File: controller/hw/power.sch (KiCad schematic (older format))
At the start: 12 parts, among them P401 WAGO255, Q401 IRFU9024, U401 Mini-360, U402 Mini-360

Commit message: Restructure files and small updates
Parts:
- added C?: C, symbol C
- added R?: 12k, symbol R
- added R?: 10k, symbol R
- added R?: R, symbol R
- added U?: TL431ACD, symbol TL431ACD
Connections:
- wire segments 40 -> 57
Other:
- note added: "Overvoltage crowbar protection"
- note added: "Triak, MT1 nahoře\nnapř. Z0103MA 5AL2"
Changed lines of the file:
@@
 	1    0    0    -1
 $EndComp
-Text HLabel 7000 1200 2    60   UnSpc ~ 0
+Text HLabel 10250 1200 2    60   UnSpc ~ 0
 +5V
 Text HLabel 7000 2600 2    60   UnSpc ~ 0
 +12V
-Text HLabel 7000 3450 2    60   UnSpc ~ 0
+Text HLabel 10250 3450 2    60   UnSpc ~ 0
 GND
 Text Notes 4950 1650 0    60   ~ 0
@@
 Connection ~ 4200 2050
 Wire Wire Line
-	4450 1800 4450 3450
+	4450 3450 4450 1800
 Wire Wire Line
 	4450 1800 4600 1800
@@
 	6300 3450 6300 2950
 Wire Wire Line
-	7000 1200 5650 1200
-Wire Wire Line
-	3050 3450 7000 3450
+	10250 1200 5650 1200
+Wire Wire Line
+	3050 3450 10250 3450
 Connection ~ 5650 3450
 Wire Wire Line
@@
 	3600 2900 3600 3450
 Connection ~ 3600 3450
+$Comp
+L TL431ACD U?
+U 1 1 5925D1B0
+P 8700 2250
+F 0 "U?" H 9088 2303 60  0000 L CNN
+F 1 "TL431ACD" H 9088 2197 60  0000 L CNN
+F 2 "" H 9550 2100 60  0001 C CNN
+F 3 "" H 9550 2100 60  0001 C CNN
+	1    8700 2250
+	1    0    0    -1
+$EndComp
+$Comp
+L R R?
+U 1 1 5925D21E
+P 8000 1950
+F 0 "R?" H 8070 1996 50  0000 L CNN
+F 1 "12k" H 8070 1905 50  0000 L CNN
+F 2 "" V 7930 1950 30  0000 C CNN
+F 3 "" H 8000 1950 30  0000 C CNN
+	1    8000 1950
+	1    0    0    -1
+$EndComp
+$Comp
+L R R?
+U 1 1 5925D25E
+P 8000 2350
+F 0 "R?" H 8070 2396 50  0000 L CNN
+F 1 "10k" H 8070 2305 50  0000 L CNN
+F 2 "" V 7930 2350 30  0000 C CNN
+F 3 "" H 8000 2350 30  0000 C CNN
+	1    8000 2350
+	1    0    0    -1
+$EndComp
+$Comp
+L R R?
+U 1 1 5925D32B
+P 8900 1600
+F 0 "R?" H 8970 1646 50  0000 L CNN
+F 1 "R" H 8970 1555 50  0000 L CNN
+F 2 "" V 8830 1600 30  0000 C CNN
+F 3 "" H 8900 1600 30  0000 C CNN
+	1    8900 1600
+	1    0    0    -1
+$EndComp
+Wire Wire Line
+	8300 2150 8000 2150
+Wire Wire Line
+	8000 2100 8000 2200
+Connection ~ 8000 2150
+Wire Wire Line
+	8000 2500 8000 2800
+Wire Wire Line
+	8000 2800 9350 2800
+Wire Wire Line
+	9000 2800 9000 2650
+Wire Wire Line
+	8550 2800 8550 3450
+Connection ~ 8550 3450
+Connection ~ 8550 2800
+Wire Wire Line
+	8700 2650 8700 2800
+Connection ~ 8700 2800
+Wire Wire Line
+	8800 2650 8800 2800
+Connection ~ 8800 2800
+Wire Wire Line
+	8900 2650 8900 2800
+Connection ~ 8900 2800
+Wire Wire Line
+	8000 1800 8000 1350
+Wire Wire Line
+	8000 1350 9850 1350
+Wire Wire Line
+	8900 1450 8900 1350
+Connection ~ 8900 1350
+Wire Wire Line
+	8900 1750 8900 1850
+Wire Wire Line
+	8900 1800 9550 1800
+Connection ~ 8900 1800
+Wire Wire Line
+	8550 1350 8550 1200
+Connection ~ 8550 1200
+Connection ~ 8550 1350
+Text Notes 7900 1100 0    60   ~ 0
+Overvoltage crowbar protection
+$Comp
+L C C?
+U 1 1 5925DDF5
+P 9350 2600
+F 0 "C?" H 9465 2646 50  0000 L CNN
+F 1 "C" H 9465 2555 50  0000 L CNN
+F 2 "" H 9388 2450 30  0000 C CNN
+F 3 "" H 9350 2600 60  0000 C CNN
+	1    9350 2600
+	1    0    0    -1
+$EndComp
+Wire Wire Line
+	9350 2450 9350 1800
+Connection ~ 9350 1800
+Wire Wire Line
+	9350 2800 9350 2750
+Connection ~ 9000 2800
+Text Notes 9900 2350 0    60   ~ 0
+Triak, MT1 nahoře\nnapř. Z0103MA 5AL2
 $EndSCHEMATC

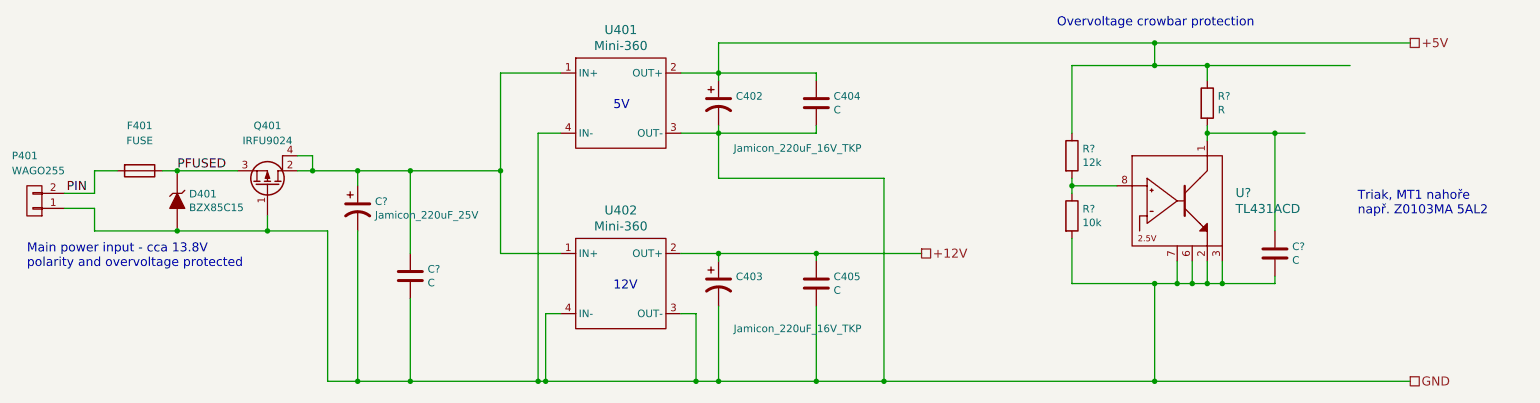
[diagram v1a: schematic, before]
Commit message: Fix voltage for SPI flash, short under one capacitor
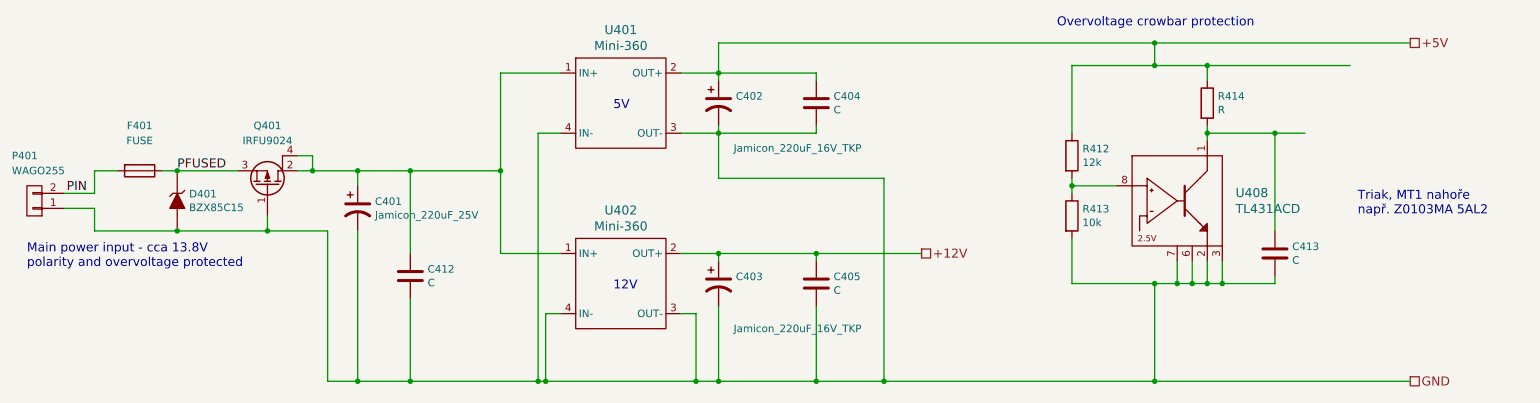
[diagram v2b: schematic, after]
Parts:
- gave numbers to parts that had none: 7
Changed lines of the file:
@@
 $EndComp
 $Comp
-L Jamicon_220uF_25V C?
+L Jamicon_220uF_25V C401
 U 1 1 5922BD9A
 P 3250 2300
-F 0 "C?" H 3365 2346 50  0000 L CNN
+F 0 "C401" H 3365 2346 50  0000 L CNN
 F 1 "Jamicon_220uF_25V" H 3365 2255 50  0000 L CNN
 F 2 "" H 3250 2300 60  0000 C CNN
@@
 $EndComp
 $Comp
-L C C?
+L C C412
 U 1 1 5922BEB6
 P 3600 2750
-F 0 "C?" H 3715 2796 50  0000 L CNN
+F 0 "C412" H 3715 2796 50  0000 L CNN
 F 1 "C" H 3715 2705 50  0000 L CNN
 F 2 "" H 3638 2600 30  0000 C CNN
@@
 Connection ~ 3600 3450
 $Comp
-L TL431ACD U?
+L TL431ACD U408
 U 1 1 5925D1B0
 P 8700 2250
-F 0 "U?" H 9088 2303 60  0000 L CNN
+F 0 "U408" H 9088 2303 60  0000 L CNN
 F 1 "TL431ACD" H 9088 2197 60  0000 L CNN
 F 2 "" H 9550 2100 60  0001 C CNN
@@
 $EndComp
 $Comp
-L R R?
+L R R412
 U 1 1 5925D21E
 P 8000 1950
-F 0 "R?" H 8070 1996 50  0000 L CNN
+F 0 "R412" H 8070 1996 50  0000 L CNN
 F 1 "12k" H 8070 1905 50  0000 L CNN
 F 2 "" V 7930 1950 30  0000 C CNN
@@
 $EndComp
 $Comp
-L R R?
+L R R413
 U 1 1 5925D25E
 P 8000 2350
-F 0 "R?" H 8070 2396 50  0000 L CNN
+F 0 "R413" H 8070 2396 50  0000 L CNN
 F 1 "10k" H 8070 2305 50  0000 L CNN
 F 2 "" V 7930 2350 30  0000 C CNN
@@
 $EndComp
 $Comp
-L R R?
+L R R414
 U 1 1 5925D32B
 P 8900 1600
-F 0 "R?" H 8970 1646 50  0000 L CNN
+F 0 "R414" H 8970 1646 50  0000 L CNN
 F 1 "R" H 8970 1555 50  0000 L CNN
 F 2 "" V 8830 1600 30  0000 C CNN
@@
 Overvoltage crowbar protection
 $Comp
-L C C?
+L C C413
 U 1 1 5925DDF5
 P 9350 2600
-F 0 "C?" H 9465 2646 50  0000 L CNN
+F 0 "C413" H 9465 2646 50  0000 L CNN
 F 1 "C" H 9465 2555 50  0000 L CNN
 F 2 "" H 9388 2450 30  0000 C CNN

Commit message: Save latest changes to sch
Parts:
- C401: footprint (none) -> th-normal:C_Radial_D8_L11.5_P3.5
- C412, C413: footprint (none) -> smd-handsolder:C_1206_HandSoldering
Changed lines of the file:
@@
 F 0 "C401" H 3365 2346 50  0000 L CNN
 F 1 "Jamicon_220uF_25V" H 3365 2255 50  0000 L CNN
-F 2 "" H 3250 2300 60  0000 C CNN
+F 2 "th-normal:C_Radial_D8_L11.5_P3.5" H 3250 2300 60  0001 C CNN
 F 3 "" H 3250 2300 60  0000 C CNN
 	1    3250 2300
@@
 F 0 "C412" H 3715 2796 50  0000 L CNN
 F 1 "C" H 3715 2705 50  0000 L CNN
-F 2 "" H 3638 2600 30  0000 C CNN
+F 2 "smd-handsolder:C_1206_HandSoldering" H 3638 2600 30  0001 C CNN
 F 3 "" H 3600 2750 60  0000 C CNN
 	1    3600 2750
@@
 F 0 "R412" H 8070 1996 50  0000 L CNN
 F 1 "12k" H 8070 1905 50  0000 L CNN
-F 2 "" V 7930 1950 30  0000 C CNN
+F 2 "" V 7930 1950 30  0001 C CNN
 F 3 "" H 8000 1950 30  0000 C CNN
 	1    8000 1950
@@
 F 0 "R413" H 8070 2396 50  0000 L CNN
 F 1 "10k" H 8070 2305 50  0000 L CNN
-F 2 "" V 7930 2350 30  0000 C CNN
+F 2 "" V 7930 2350 30  0001 C CNN
 F 3 "" H 8000 2350 30  0000 C CNN
 	1    8000 2350
@@
 F 0 "R414" H 8970 1646 50  0000 L CNN
 F 1 "R" H 8970 1555 50  0000 L CNN
-F 2 "" V 8830 1600 30  0000 C CNN
+F 2 "" V 8830 1600 30  0001 C CNN
 F 3 "" H 8900 1600 30  0000 C CNN
 	1    8900 1600
@@
 F 0 "C413" H 9465 2646 50  0000 L CNN
 F 1 "C" H 9465 2555 50  0000 L CNN
-F 2 "" H 9388 2450 30  0000 C CNN
+F 2 "smd-handsolder:C_1206_HandSoldering" H 9388 2450 30  0001 C CNN
 F 3 "" H 9350 2600 60  0000 C CNN
 	1    9350 2600

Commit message: Compilability using embc lm4f, fixes to TX_EN switching
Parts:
- C401: symbol Jamicon_220uF_25V -> capacitors:Jamicon_220uF_25V
- C402, C403: symbol Jamicon_220uF_16V_TKP -> capacitors:Jamicon_220uF_16V_TKP
- C404, C405, C412, C413: symbol C -> simple:C
- D401: symbol BZX85C15 -> discrete:BZX85C15
- F401: symbol FUSE -> templates:FUSE
- P401: symbol CONN_01X02 -> connectors:CONN_01X02
- Q401: symbol IRFU9024 -> transistors:IRFU9024
- R412, R413, R414: symbol R -> simple:R
- U401, U402: symbol Mini-360 -> power:Mini-360
- U408: symbol TL431ACD -> simple:TL431ACD
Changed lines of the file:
@@
-EESchema Schematic File Version 2
-LIBS:74xx
-LIBS:boards
-LIBS:buttons
-LIBS:capacitors
-LIBS:connectors
-LIBS:cpu
-LIBS:discrete
-LIBS:drivers
-LIBS:ic
-LIBS:mspower
-LIBS:opto
-LIBS:passives
-LIBS:power
-LIBS:relay
-LIBS:rf
-LIBS:simple
-LIBS:transistors
-LIBS:templates
+EESchema Schematic File Version 4
 LIBS:dvernik-cache
 EELAYER 26 0
@@
 $EndDescr
 $Comp
-L Mini-360 U401
+L power:Mini-360 U401
 U 1 1 590E228F
 P 5000 1600
@@
 $EndComp
 $Comp
-L C C404
+L simple:C C404
 U 1 1 590E22AE
 P 6300 1600
@@
 $EndComp
 $Comp
-L FUSE F401
+L templates:FUSE F401
 U 1 1 590E22B5
 P 1800 2050
@@
 $EndComp
 $Comp
-L IRFU9024 Q401
+L transistors:IRFU9024 Q401
 U 1 1 590E22BC
 P 2650 2150
@@
 $EndComp
 $Comp
-L CONN_01X02 P401
+L connectors:CONN_01X02 P401
 U 1 1 590E22C3
 P 1100 2250
@@
 Main power input - cca 13.8V\npolarity and overvoltage protected
 $Comp
-L Jamicon_220uF_16V_TKP C402
+L capacitors:Jamicon_220uF_16V_TKP C402
 U 1 1 590E22CB
 P 5650 1600
@@
 $EndComp
 $Comp
-L C C405
+L simple:C C405
 U 1 1 590E2568
 P 6300 2800
@@
 12V
 $Comp
-L BZX85C15 D401
+L discrete:BZX85C15 D401
 U 1 1 590E6F05
 P 2050 2250
@@
 $EndComp
 $Comp
-L Jamicon_220uF_16V_TKP C403
+L capacitors:Jamicon_220uF_16V_TKP C403
 U 1 1 590E256E
 P 5650 2800
@@
 PFUSED
 $Comp
-L Mini-360 U402
+L power:Mini-360 U402
 U 1 1 5922A582
 P 5000 2800
@@
 $EndComp
 $Comp
-L Jamicon_220uF_25V C401
+L capacitors:Jamicon_220uF_25V C401
 U 1 1 5922BD9A
 P 3250 2300
@@
 $EndComp
 $Comp
-L C C412
+L simple:C C412
 U 1 1 5922BEB6
 P 3600 2750
@@
 Connection ~ 3600 3450
 $Comp
-L TL431ACD U408
+L simple:TL431ACD U408
 U 1 1 5925D1B0
 P 8700 2250
@@
 $EndComp
 $Comp
-L R R412
+L simple:R R412
 U 1 1 5925D21E
 P 8000 1950
@@
 $EndComp
 $Comp
-L R R413
+L simple:R R413
 U 1 1 5925D25E
 P 8000 2350
@@
 $EndComp
 $Comp
-L R R414
+L simple:R R414
 U 1 1 5925D32B
 P 8900 1600
@@
 Overvoltage crowbar protection
 $Comp
-L C C413
+L simple:C C413
 U 1 1 5925DDF5
 P 9350 2600

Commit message: WIP Still working in 3.3 - 5V interface issues
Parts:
- R412: footprint (none) -> smd-handsolder:R_1206_HandSoldering
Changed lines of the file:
@@
 F 0 "R412" H 8070 1996 50  0000 L CNN
 F 1 "12k" H 8070 1905 50  0000 L CNN
-F 2 "" V 7930 1950 30  0001 C CNN
+F 2 "smd-handsolder:R_1206_HandSoldering" V 7930 1950 30  0001 C CNN
 F 3 "" H 8000 1950 30  0000 C CNN
 	1    8000 1950

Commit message: schematic improvements (door state pin for controller, fixes)
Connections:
- wire segments 57 -> 90
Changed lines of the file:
@@
 $EndComp
 Wire Wire Line
-	5400 1400 6300 1400
-Wire Wire Line
-	5650 1200 5650 1450
-Wire Wire Line
-	5400 1800 6300 1800
-Wire Wire Line
-	5650 1750 5650 2100
-Wire Wire Line
-	2850 2050 4200 2050
+	5400 1400 5650 1400
+Wire Wire Line
+	5650 1200 5650 1400
+Wire Wire Line
+	5400 1800 5650 1800
+Wire Wire Line
+	5650 1750 5650 1800
+Wire Wire Line
+	2850 2050 2950 2050
 Connection ~ 5650 1400
 Connection ~ 5650 1800
@@
 	6300 1800 6300 1750
 Wire Wire Line
-	1950 2050 2450 2050
+	1950 2050 2050 2050
 Wire Wire Line
 	2850 1950 2950 1950
@@
 	1500 2200 1500 2050
 Wire Wire Line
-	4200 1400 4200 2600
+	4200 1400 4200 2050
 Wire Wire Line
 	4200 1400 4600 1400
@@
 	6300 3450 6300 2950
 Wire Wire Line
-	10250 1200 5650 1200
-Wire Wire Line
-	3050 3450 10250 3450
+	10250 1200 8550 1200
+Wire Wire Line
+	3050 3450 3250 3450
 Connection ~ 5650 3450
 Wire Wire Line
@@
 	3050 2450 3050 3450
 Wire Wire Line
-	1500 2450 3050 2450
+	1500 2450 2050 2450
 Connection ~ 4450 3450
 Connection ~ 6300 3450
@@
 	4200 2600 4600 2600
 Wire Wire Line
-	5400 2600 7000 2600
+	5400 2600 5650 2600
 Wire Wire Line
 	4600 3000 4500 3000
@@
 	8300 2150 8000 2150
 Wire Wire Line
-	8000 2100 8000 2200
+	8000 2100 8000 2150
 Connection ~ 8000 2150
 Wire Wire Line
 	8000 2500 8000 2800
 Wire Wire Line
-	8000 2800 9350 2800
+	8000 2800 8550 2800
 Wire Wire Line
 	9000 2800 9000 2650
@@
 	8000 1800 8000 1350
 Wire Wire Line
-	8000 1350 9850 1350
+	8000 1350 8550 1350
 Wire Wire Line
 	8900 1450 8900 1350
 Connection ~ 8900 1350
 Wire Wire Line
-	8900 1750 8900 1850
-Wire Wire Line
-	8900 1800 9550 1800
+	8900 1750 8900 1800
+Wire Wire Line
+	8900 1800 9350 1800
 Connection ~ 8900 1800
 Wire Wire Line
@@
 Text Notes 9900 2350 0    60   ~ 0
 Triak, MT1 nahoře\nnapř. Z0103MA 5AL2
+Wire Wire Line
+	5650 1400 6300 1400
+Wire Wire Line
+	5650 1400 5650 1450
+Wire Wire Line
+	5650 1800 6300 1800
+Wire Wire Line
+	5650 1800 5650 2100
+Wire Wire Line
+	2950 2050 3250 2050
+Wire Wire Line
+	2650 2450 3050 2450
+Wire Wire Line
+	4200 2050 4200 2600
+Wire Wire Line
+	5650 3450 6300 3450
+Wire Wire Line
+	6750 3450 8550 3450
+Wire Wire Line
+	2050 2450 2650 2450
+Wire Wire Line
+	2050 2050 2450 2050
+Wire Wire Line
+	4450 3450 4500 3450
+Wire Wire Line
+	6300 3450 6750 3450
+Wire Wire Line
+	5650 2600 6300 2600
+Wire Wire Line
+	6300 2600 7000 2600
+Wire Wire Line
+	4500 3450 5500 3450
+Wire Wire Line
+	5500 3450 5650 3450
+Wire Wire Line
+	3250 2050 3600 2050
+Wire Wire Line
+	3250 3450 3600 3450
+Wire Wire Line
+	3600 2050 4200 2050
+Wire Wire Line
+	3600 3450 4450 3450
+Wire Wire Line
+	8000 2150 8000 2200
+Wire Wire Line
+	8550 3450 10250 3450
+Wire Wire Line
+	8550 2800 8700 2800
+Wire Wire Line
+	8700 2800 8800 2800
+Wire Wire Line
+	8800 2800 8900 2800
+Wire Wire Line
+	8900 2800 9000 2800
+Wire Wire Line
+	8900 1350 9850 1350
+Wire Wire Line
+	8900 1800 8900 1850
+Wire Wire Line
+	8550 1200 5650 1200
+Wire Wire Line
+	8550 1350 8900 1350
+Wire Wire Line
+	9350 1800 9550 1800
+Wire Wire Line
+	9000 2800 9350 2800
 $EndSCHEMATC
